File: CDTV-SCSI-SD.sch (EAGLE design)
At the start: 25 parts, among them CN1 CDTV-EXPANSION, IC1 74HC245N, IC2 WD33C93A, X1 057-050-1

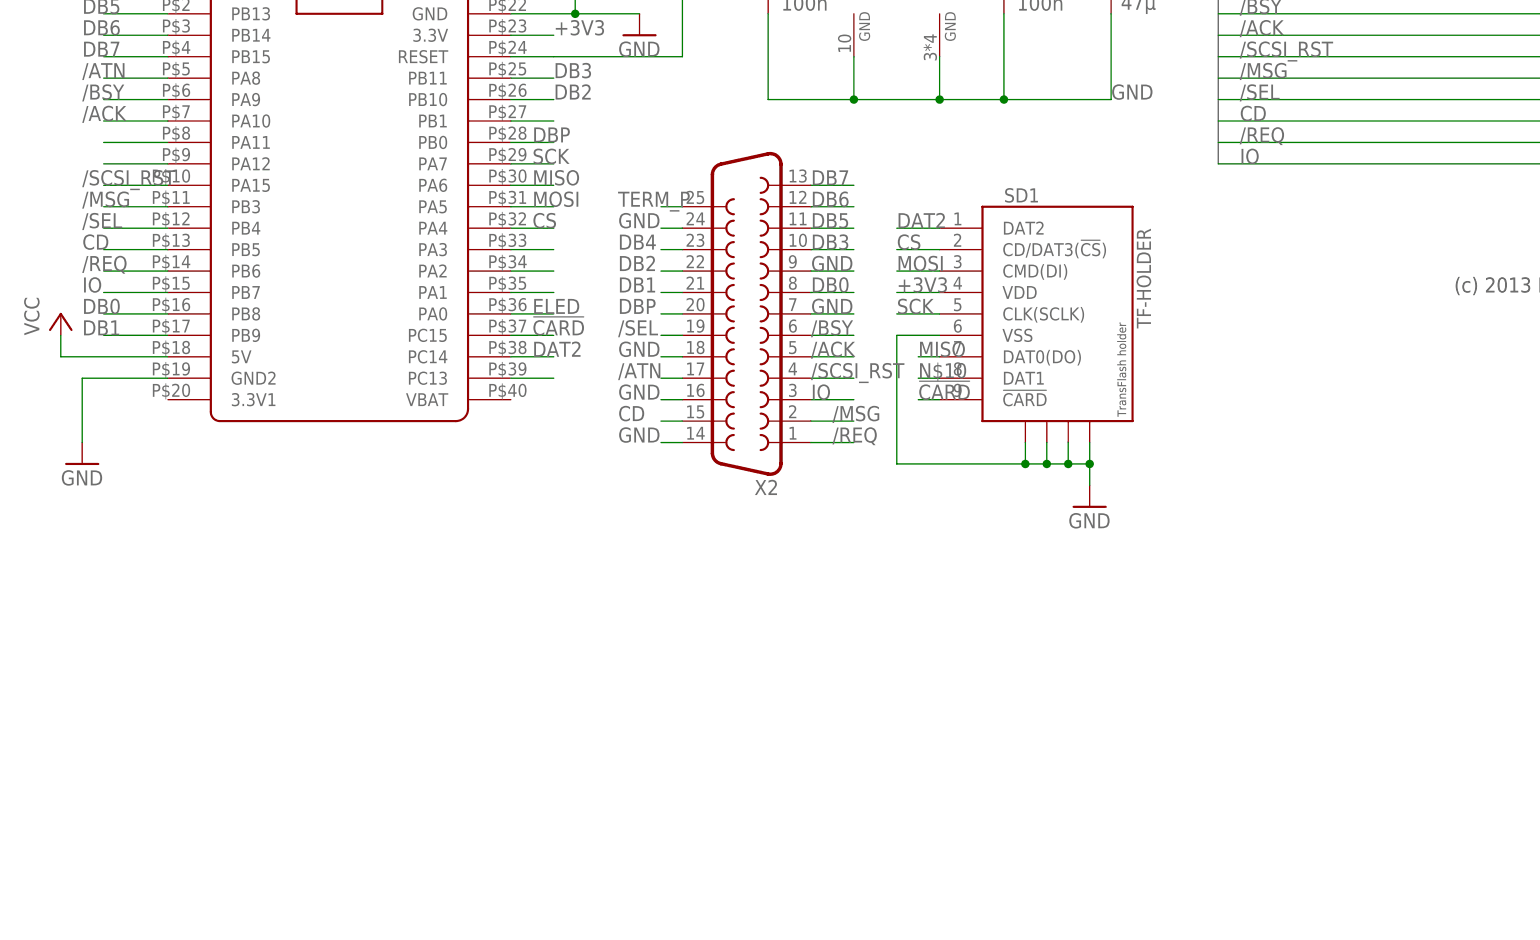
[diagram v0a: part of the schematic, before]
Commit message: (fix), db25 was male instead of female
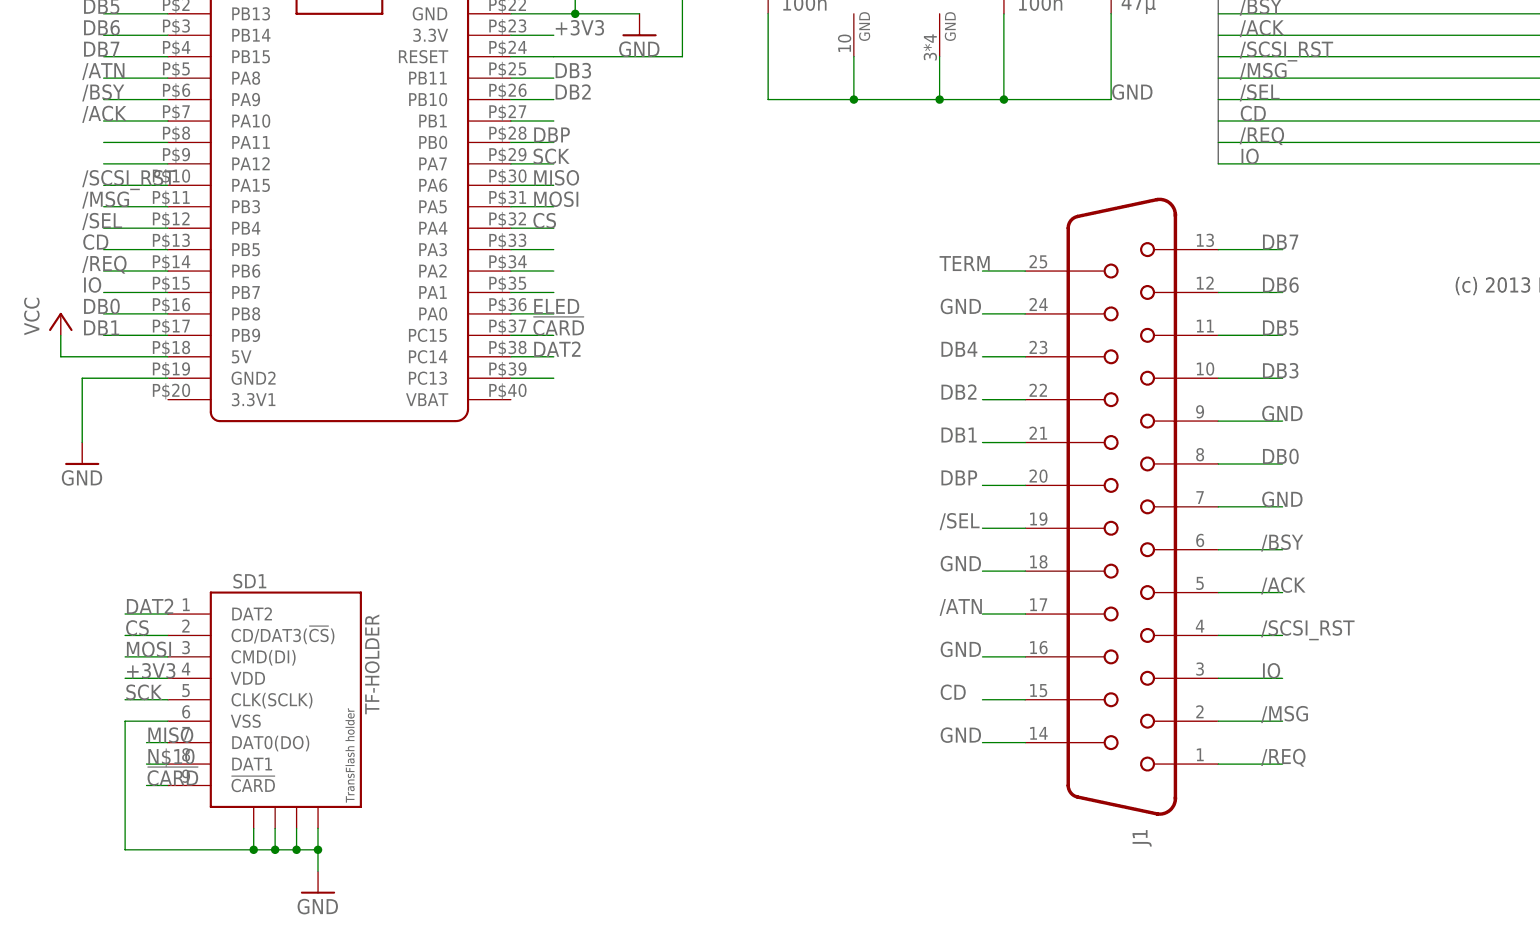
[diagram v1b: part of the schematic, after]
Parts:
- removed X2: (no value), SparkFun:F25H
- added J1: (no value), InputOutputIO (rev18a):61802529321
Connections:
- new net TERM: J1.25
- net /ACK: now also J1.5; no longer X2.5
- net /ATN: now also J1.17; no longer X2.17
- net /BSY: now also J1.6; no longer X2.6
- net /MSG: now also J1.2; no longer X2.2
- net /REQ: now also J1.1; no longer X2.1
- net /SCSI_RST: now also J1.4; no longer X2.4
- net /SEL: now also J1.19; no longer X2.19
- net CD: now also J1.15; no longer X2.15
- net DB0: now also J1.8; no longer X2.8
- net DB1: now also J1.21; no longer X2.21
- net DB2: now also J1.22; no longer X2.22
- net DB3: now also J1.10; no longer X2.10
- net DB4: now also J1.23; no longer X2.23
- net DB5: now also J1.11; no longer X2.11
- net DB6: now also J1.12; no longer X2.12
- net DB7: now also J1.13; no longer X2.13
- net DBP: now also J1.20; no longer X2.20
- net GND: now also J1.14, J1.16, J1.18, J1.24, J1.7, J1.9; no longer X2.14, X2.16, X2.18, X2.24, X2.7, X2.9
- net IO: now also J1.3; no longer X2.3
- net TERM_P: no longer X2.25
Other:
- moved on the sheet: SD1

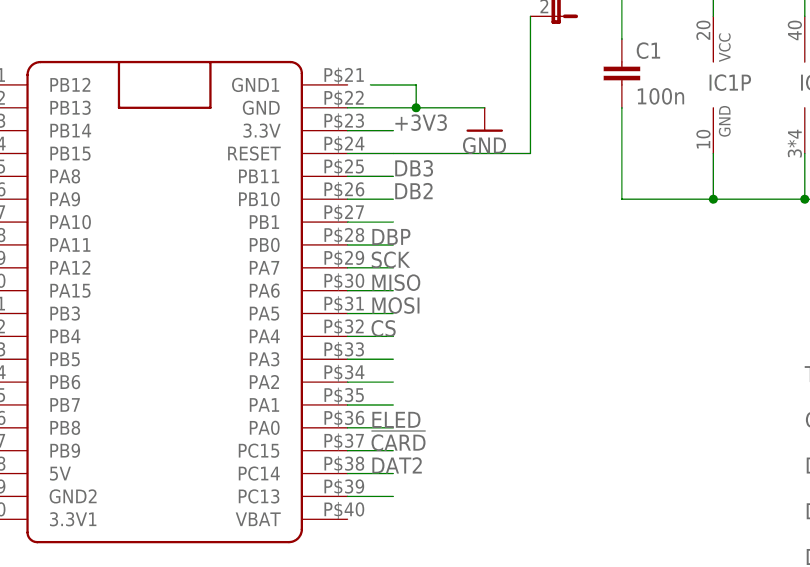
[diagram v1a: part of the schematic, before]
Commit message: (fix), MOSI and SCK were switched
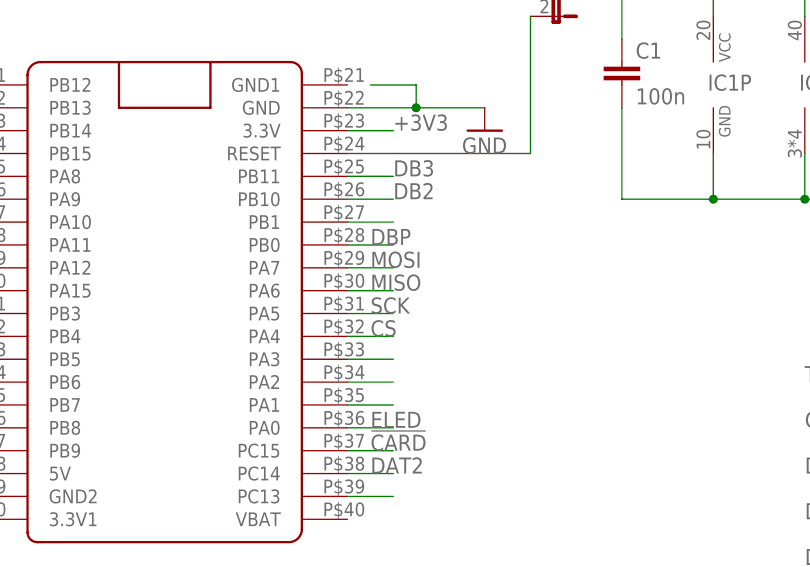
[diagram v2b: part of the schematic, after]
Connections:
- net MOSI: now also U$1.PA7; no longer U$1.PA5
- net SCK: now also U$1.PA5; no longer U$1.PA7
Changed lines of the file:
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@@
 <net name="MOSI" class="0">
-<segment>
-<pinref part="U$1" gate="G$1" pin="PA5"/>
-<wire x1="-5.08" y1="-106.68" x2="0" y2="-106.68" width="0.1524" layer="91"/>
-<label x="-2.54" y="-106.68" size="1.778" layer="95"/>
-</segment>
 <segment>
 <pinref part="SD1" gate="G$1" pin="CMD(DI)"/>
 <wire x1="-45.72" y1="-160.02" x2="-50.8" y2="-160.02" width="0.1524" layer="91"/>
 <label x="-50.8" y="-160.02" size="1.778" layer="95"/>
+</segment>
+<segment>
+<pinref part="U$1" gate="G$1" pin="PA7"/>
+<wire x1="-5.08" y1="-101.6" x2="0" y2="-101.6" width="0.1524" layer="91"/>
+<label x="-2.54" y="-101.6" size="1.778" layer="95"/>
 </segment>
 </net>
@@
 <net name="SCK" class="0">
 <segment>
-<pinref part="U$1" gate="G$1" pin="PA7"/>
-<wire x1="-5.08" y1="-101.6" x2="0" y2="-101.6" width="0.1524" layer="91"/>
-<label x="-2.54" y="-101.6" size="1.778" layer="95"/>
-</segment>
-<segment>
 <pinref part="SD1" gate="G$1" pin="CLK(SCLK)"/>
 <wire x1="-45.72" y1="-165.1" x2="-50.8" y2="-165.1" width="0.1524" layer="91"/>
 <label x="-50.8" y="-165.1" size="1.778" layer="95"/>
 </segment>
+<segment>
+<pinref part="U$1" gate="G$1" pin="PA5"/>
+<wire x1="-5.08" y1="-106.68" x2="0" y2="-106.68" width="0.1524" layer="91"/>
+<label x="-2.54" y="-106.68" size="1.778" layer="95"/>
+</segment>
 </net>
